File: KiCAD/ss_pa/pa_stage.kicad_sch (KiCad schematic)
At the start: 52 parts, among them J1 Conn_Coaxial_Small, J2 Screw_Terminal_01x02, J3 Conn_Coaxial_Small, Q2 BS170, Q3 IRF510, Q4 IRF510, Q6 BS170, T201 BN61-2402, T202 BN61-2402, T203 T50-43, T204 BN43-202

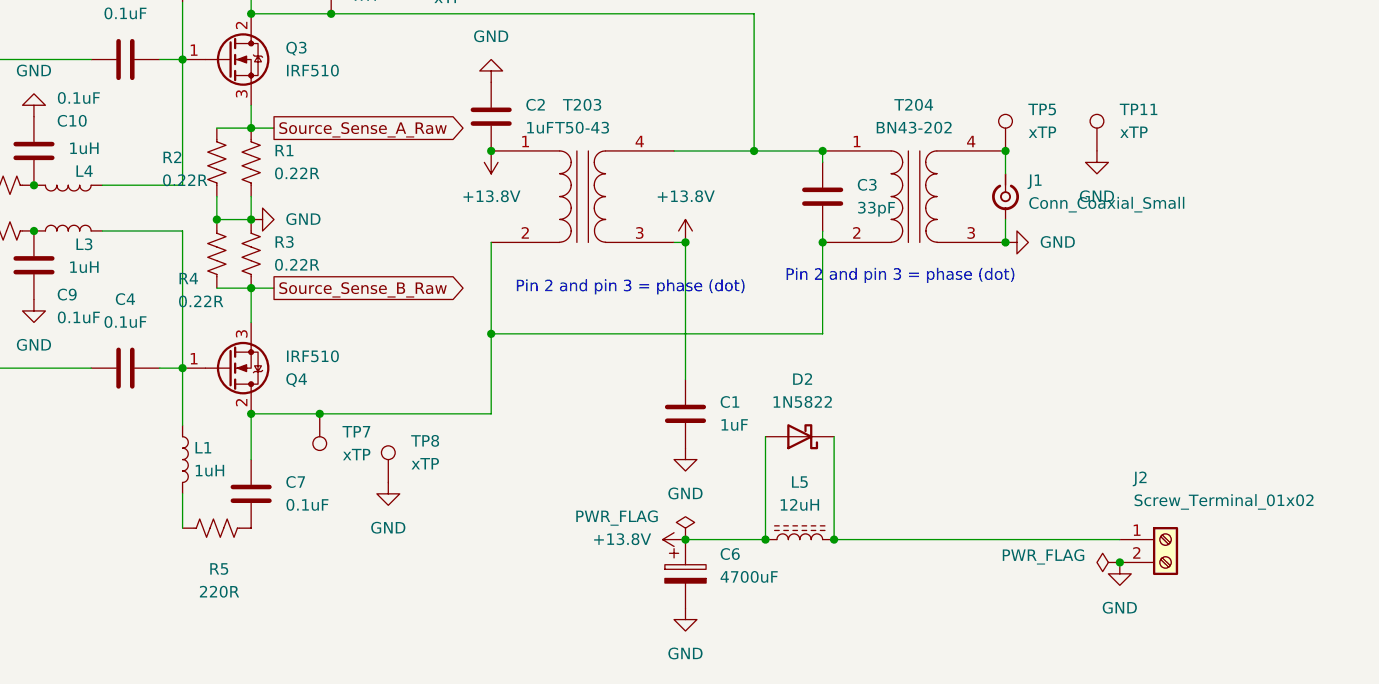
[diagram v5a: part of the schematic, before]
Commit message: revD: footprint pass across all boards + ss_pa fault-chain fix + LLM review brief
- New tools/assign_misc_footprints.py: lib_id-keyed footprint assigner
  (resistors, screw terminals, pin headers, LT1054); mirrors cap-script
  safe-write (UTF-8 no BOM, no CRLF translation).
- tools/assign_cap_footprints.py: added 0.47uF -> C_Rect_L7.0mm case.
- Ran both scripts across analog, ss_pa, Output LPF, frontpanel,
  protoshield, and shelved power board. ~100 fills; details in diffs.
- ss_pa: R1-R4 (0.22 ohm source sense) upgraded to 2W Yageo RSF200
  with DIN0516 L15.5mm/P20.32mm footprint; Value tagged "0.22R 2W".
  R15/R16 confirmed 1/4W (DIN0207) for BS170 source degeneration.
- analog/power: R44 15R 5W horizontal, P30.48mm footprint.
- ss_pa fault chain (from external LLM review): R21/R22 raised
  10K -> 100K to restore self-latching loop gain; new R26 = 100K
  across C12 so cap discharges between power cycles (reliable reset).
  R26 footprint pending.
- Documentation/revD_llm_review_brief.md: new, comprehensive system
  description for external LLM deep-dive (function, component values,
  power dissipation, design flaws). References all five board netlists.

Co-Authored-By: Claude Opus 4.7 <noreply@anthropic.com>
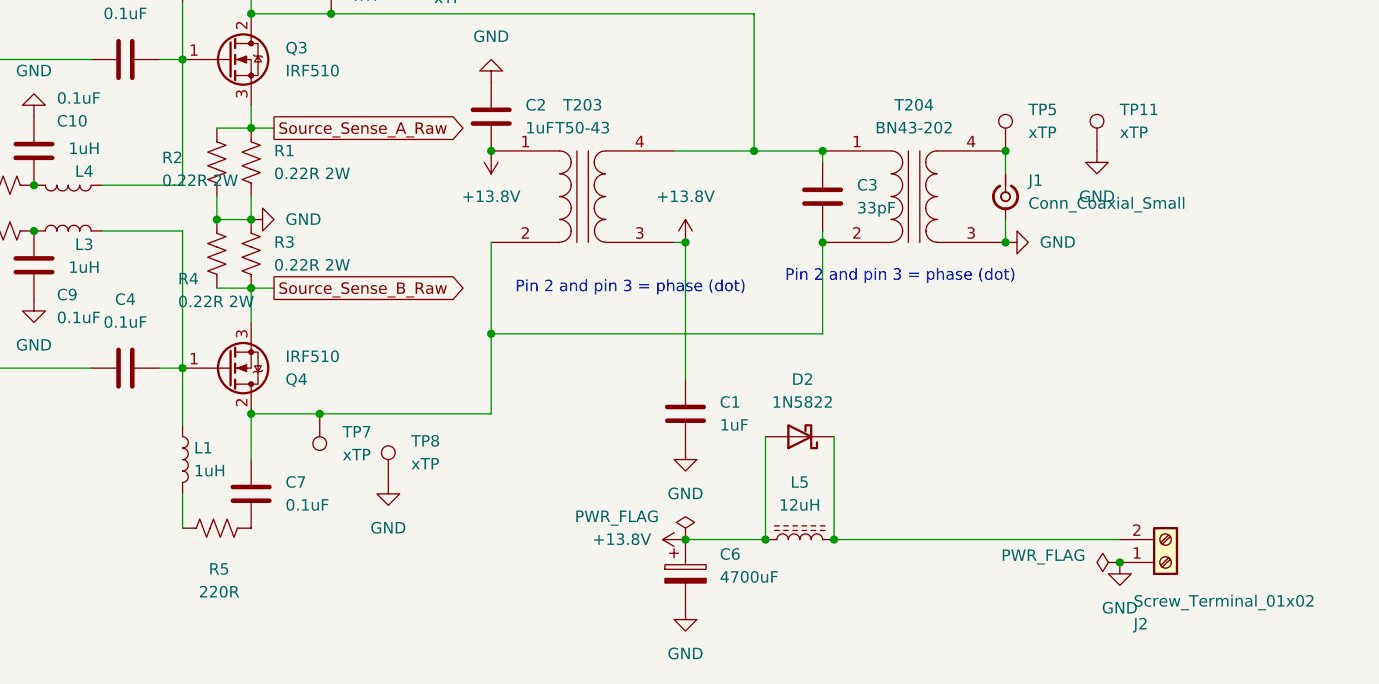
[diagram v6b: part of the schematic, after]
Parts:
- R1, R2, R3, R4: value 0.22R -> 0.22R 2W; footprint Resistor_THT:R_Axial_DIN0207_L6.3mm_D2.5mm_P10.16mm_Horizontal -> Resistor_THT:R_Axial_DIN0516_L15.5mm_D5.0mm_P20.32mm_Horizontal
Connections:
- net GND: now also J2.1 (Pin_1); no longer J2.2 (Pin_2)
- net at D2.1 (K), L5.2: now also J2.2 (Pin_2); no longer J2.1 (Pin_1)
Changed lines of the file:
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@@
 	)
 	(symbol
+		(lib_id "Connector:Screw_Terminal_01x02")
+		(at 262.89 130.81 0)
+		(mirror x)
+		(unit 1)
+		(body_style 1)
+		(exclude_from_sim no)
+		(in_bom yes)
+		(on_board yes)
+		(in_pos_files yes)
+		(dnp no)
+		(property "Reference" "J2"
+			(at 259.334 137.668 0)
+			(show_name no)
+			(do_not_autoplace no)
+			(effects
+				(font
+					(size 1.27 1.27)
+				)
+				(justify left)
+			)
+		)
+		(property "Value" "Screw_Terminal_01x02"
+			(at 259.334 135.128 0)
+			(show_name no)
+			(do_not_autoplace no)
+			(effects
+				(font
+					(size 1.27 1.27)
+				)
+				(justify left)
+			)
+		)
+		(property "Footprint" "TerminalBlock_Phoenix:TerminalBlock_Phoenix_MKDS-1,5-2_1x02_P5.00mm_Horizontal"
+			(at 262.89 130.81 0)
+			(hide yes)
+			(show_name no)
+			(do_not_autoplace no)
+			(effects
+				(font
+					(size 1.27 1.27)
+				)
+			)
+		)
+		(property "Datasheet" ""
+			(at 262.89 130.81 0)
+			(hide yes)
+			(show_name no)
+			(do_not_autoplace no)
+			(effects
+				(font
+					(size 1.27 1.27)
+				)
+			)
+		)
+		(property "Description" "Generic screw terminal, single row, 01x02, script generated (kicad-library-utils/schlib/autogen/connector/)"
+			(at 262.89 130.81 0)
+			(hide yes)
+			(show_name no)
+			(do_not_autoplace no)
+			(effects
+				(font
+					(size 1.27 1.27)
+				)
+			)
+		)
+		(pin "1"
+		)
+		(pin "2"
+		)
+		(instances
+			(project "ss_pa"
+				(path "/7b9fe991-54d6-43c4-a637-0ed9ee982c42/6995ca2b-35a4-4871-8cf2-3a0067e62105"
+					(reference "J2")
+					(unit 1)
+				)
+			)
+		)
+	)
+	(symbol
 		(lib_id "Device:R_US")
 		(at 157.48 57.15 90)
@@
 			)
 		)
-		(property "Value" "0.22R"
+		(property "Value" "0.22R 2W"
 			(at 153.162 101.854 0)
 			(show_name no)
@@
 			)
 		)
-		(property "Footprint" "Resistor_THT:R_Axial_DIN0207_L6.3mm_D2.5mm_P10.16mm_Horizontal"
+		(property "Footprint" "Resistor_THT:R_Axial_DIN0516_L15.5mm_D5.0mm_P20.32mm_Horizontal"
 			(at 158.496 96.774 90)
 			(hide yes)
@@
 			)
 		)
-		(property "Value" "0.22R"
+		(property "Value" "0.22R 2W"
 			(at 163.83 97.7899 0)
 			(show_name no)
@@
 			)
 		)
-		(property "Footprint" "Resistor_THT:R_Axial_DIN0207_L6.3mm_D2.5mm_P10.16mm_Horizontal"
+		(property "Footprint" "Resistor_THT:R_Axial_DIN0516_L15.5mm_D5.0mm_P20.32mm_Horizontal"
 			(at 162.306 96.774 90)
 			(hide yes)
@@
 			)
 		)
-		(property "Value" "0.22R"
+		(property "Value" "0.22R 2W"
 			(at 163.83 87.6299 0)
 			(show_name no)
@@
 			)
 		)
-		(property "Footprint" "Resistor_THT:R_Axial_DIN0207_L6.3mm_D2.5mm_P10.16mm_Horizontal"
+		(property "Footprint" "Resistor_THT:R_Axial_DIN0516_L15.5mm_D5.0mm_P20.32mm_Horizontal"
 			(at 162.306 86.614 90)
 			(hide yes)
@@
 			)
 		)
-		(property "Value" "0.22R"
+		(property "Value" "0.22R 2W"
 			(at 151.384 88.392 0)
 			(show_name no)
@@
 			)
 		)
-		(property "Footprint" "Resistor_THT:R_Axial_DIN0207_L6.3mm_D2.5mm_P10.16mm_Horizontal"
+		(property "Footprint" "Resistor_THT:R_Axial_DIN0516_L15.5mm_D5.0mm_P20.32mm_Horizontal"
 			(at 158.496 86.614 90)
 			(hide yes)
@@
 					(unit 1)
 				)
-			)
-		)
-	)
-	(symbol
-		(lib_id "Connector:Screw_Terminal_01x02")
-		(at 262.89 128.27 0)
-		(unit 1)
-		(body_style 1)
-		(exclude_from_sim no)
-		(in_bom yes)
-		(on_board yes)
-		(in_pos_files yes)
-		(dnp no)
-		(property "Reference" "J2"
-			(at 259.334 121.412 0)
-			(show_name no)
-			(do_not_autoplace no)
-			(effects
-				(font
-					(size 1.27 1.27)
-				)
-				(justify left)
-			)
-		)
-		(property "Value" "Screw_Terminal_01x02"
-			(at 259.334 123.952 0)
-			(show_name no)
-			(do_not_autoplace no)
-			(effects
-				(font
-					(size 1.27 1.27)
-				)
-				(justify left)
-			)
-		)
-		(property "Footprint" "TerminalBlock_Phoenix:TerminalBlock_Phoenix_MKDS-1,5-2_1x02_P5.00mm_Horizontal"
-			(at 262.89 128.27 0)
-			(hide yes)
-			(show_name no)
-			(do_not_autoplace no)
-			(effects
-				(font
-					(size 1.27 1.27)
-				)
-			)
-		)
-		(property "Datasheet" ""
-			(at 262.89 128.27 0)
-			(hide yes)
-			(show_name no)
-			(do_not_autoplace no)
-			(effects
-				(font
-					(size 1.27 1.27)
-				)
-			)
-		)
-		(property "Description" "Generic screw terminal, single row, 01x02, script generated (kicad-library-utils/schlib/autogen/connector/)"
-			(at 262.89 128.27 0)
-			(hide yes)
-			(show_name no)
-			(do_not_autoplace no)
-			(effects
-				(font
-					(size 1.27 1.27)
-				)
-			)
-		)
-		(pin "1"
-		)
-		(pin "2"
-		)
-		(instances
-			(project "ss_pa"
-				(path "/7b9fe991-54d6-43c4-a637-0ed9ee982c42/6995ca2b-35a4-4871-8cf2-3a0067e62105"
-					(reference "J2")
-					(unit 1)
-				)

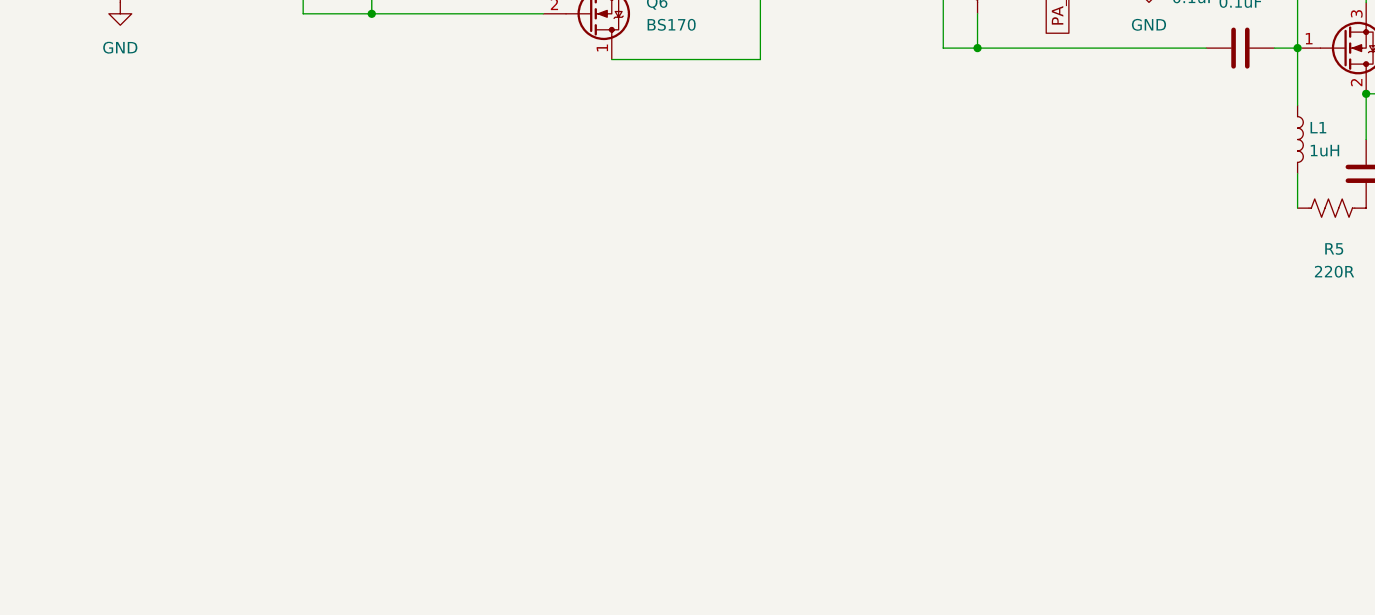
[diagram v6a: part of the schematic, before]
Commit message: revD: U18 heartbeat RC reset + fault_shutdown migrated to analog
- arduino.kicad_sch: R48 10K + C14 10uF RC on U18 RST_A holds
  CD14538B heartbeat watchdog in reset ~70-120ms during Metro boot,
  preventing SS_PWR_RLY / SS_PA_INRUSH false-energize while PCF8575
  defaults HIGH on its outputs
- fault_shutdown.kicad_sch (new): LM393 overcurrent trip +
  CD74HC4066 bias switch + V_REF latch migrated from ss_pa to
  analog so FAULT_N stays off the umbilical; co-located with the
  Metro that reads it. Ref numbers +200 to avoid collision with
  pre-existing analog refs
- analog.kicad_sch: adds Fault_Shutdown sub-sheet reference (page 11)
- ss_pa: fault_shutdown sheet reference removed; ss_pa.net reflects
  the component loss (eliminates ss_pa U3 LM2936 LDO and +5V rail
  dependency)
- pa_stage.kicad_sch: R1-R4 bumped to 2W (RSF200JT-73-0R22) with
  DIN0516 L15.5mm footprint; footprint cleanup pass
- power.kicad_sch: 4.7R dummy bumped to 4.7R 10W with Axial_Power
  L25.0mm W9.0mm P30.48mm footprint

Co-Authored-By: Claude Opus 4.7 <noreply@anthropic.com>
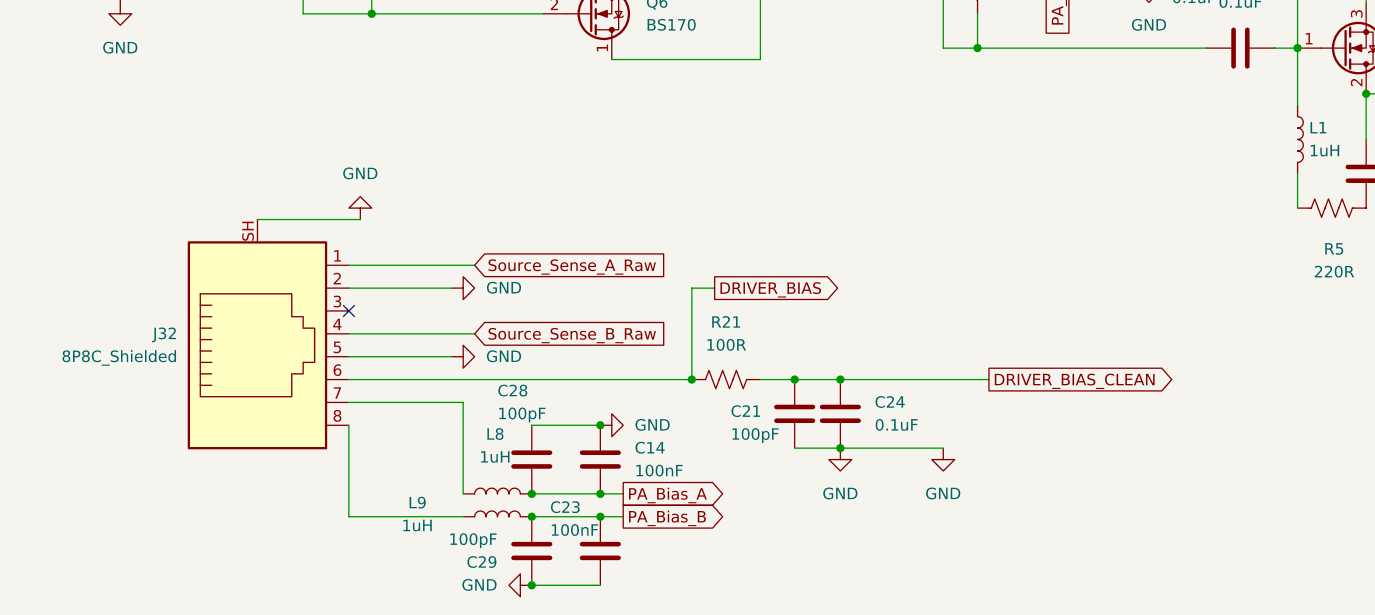
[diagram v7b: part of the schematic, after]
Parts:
- added C14, C23: 100nF, Capacitor_THT:C_Disc_D5.0mm_W2.5mm_P5.00mm, symbol Device:C
- added C21, C28, C29: 100pF, Capacitor_THT:C_Rect_L7.0mm_W3.5mm_P5.00mm, symbol Device:C
- added C24: 0.1uF, Capacitor_THT:C_Disc_D5.0mm_W2.5mm_P5.00mm, symbol Device:C
- added J32: 8P8C_Shielded, xmitter:Amphenol_RJE1D-188_Horizontal_Shielded, symbol Connector:8P8C_Shielded
- added L8, L9: 1uH, Inductor_THT:L_Axial_L5.3mm_D2.2mm_P2.54mm_Vertical_Vishay_IM-1, symbol Device:L
- added R21: 100R, Resistor_THT:R_Axial_DIN0207_L6.3mm_D2.5mm_P10.16mm_Horizontal, symbol Device:R_US
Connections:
- net DRIVER_BIAS_CLEAN: now also C21.1, C24.1, R21.2
- net GND: now also C14.1, C21.2, C23.2, C24.2, C28.1, C29.1, J32.2, J32.5, J32.SH
- net PA_Bias_A: now also C14.2, C28.2, L8.2
- net PA_Bias_B: now also C23.1, C29.2, L9.2
- net Source_Sense_A_Raw: now also J32.1
- net Source_Sense_B_Raw: now also J32.4
- new net: J32.7, L8.1
- new net: J32.8, L9.1
- new net DRIVER_BIAS: J32.6, R21.1
- no-connect marks 0 -> 1
